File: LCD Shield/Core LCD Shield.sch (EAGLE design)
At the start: 8 parts, among them IC1 MC33269T-5.0, J1 TWIG_2.0-DIP-FEMALE

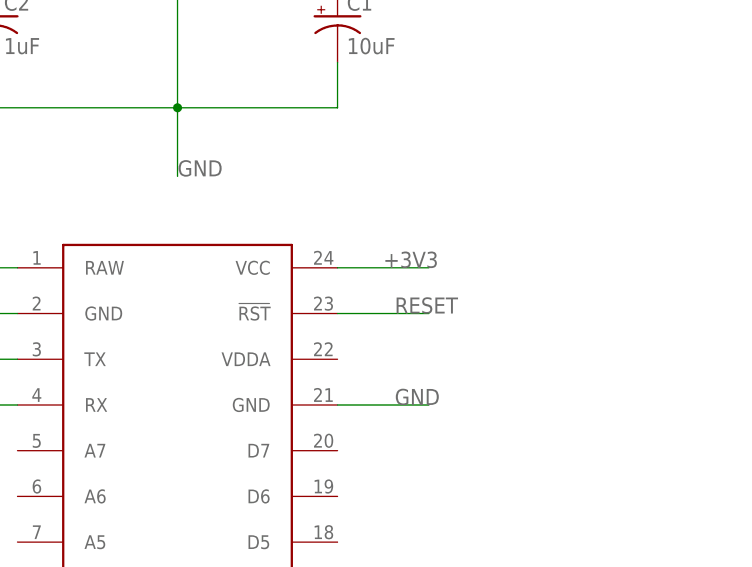
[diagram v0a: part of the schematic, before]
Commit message: Reviewed LCD Shield
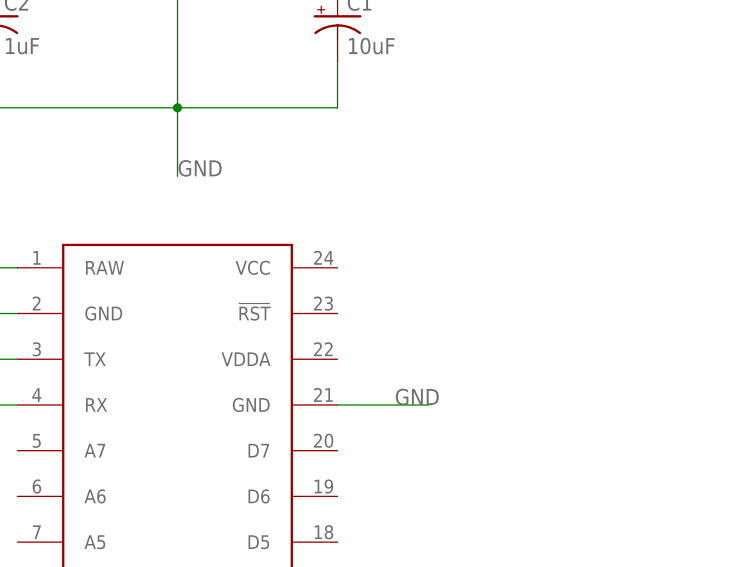
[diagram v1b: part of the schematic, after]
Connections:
- removed net +3V3: U$1.VCC
- removed net RESET: U$1.!RST
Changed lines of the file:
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@@
 <segment>
 <pinref part="IC1" gate="G$1" pin="ADJ"/>
-<wire x1="109.22" y1="124.46" x2="109.22" y2="111.76" width="0.2032" layer="91"/>
+<wire x1="109.22" y1="124.46" x2="109.22" y2="111.76" width="0.1524" layer="91"/>
 <label x="109.22" y="104.14" size="1.778" layer="95"/>
 <pinref part="C2" gate="G$1" pin="-"/>
-<wire x1="109.22" y1="111.76" x2="109.22" y2="104.14" width="0.2032" layer="91"/>
-<wire x1="88.9" y1="116.84" x2="88.9" y2="111.76" width="0.2032" layer="91"/>
-<wire x1="88.9" y1="111.76" x2="109.22" y2="111.76" width="0.2032" layer="91"/>
-<wire x1="109.22" y1="111.76" x2="127" y2="111.76" width="0.2032" layer="91"/>
+<wire x1="109.22" y1="111.76" x2="109.22" y2="104.14" width="0.1524" layer="91"/>
+<wire x1="88.9" y1="116.84" x2="88.9" y2="111.76" width="0.1524" layer="91"/>
+<wire x1="88.9" y1="111.76" x2="109.22" y2="111.76" width="0.1524" layer="91"/>
+<wire x1="109.22" y1="111.76" x2="127" y2="111.76" width="0.1524" layer="91"/>
 <pinref part="C1" gate="G$1" pin="-"/>
-<wire x1="127" y1="111.76" x2="127" y2="116.84" width="0.2032" layer="91"/>
+<wire x1="127" y1="111.76" x2="127" y2="116.84" width="0.1524" layer="91"/>
 <junction x="109.22" y="111.76"/>
 </segment>
 <segment>
 <pinref part="CN1" gate="G$1" pin="1"/>
-<wire x1="43.18" y1="121.92" x2="30.48" y2="121.92" width="0.2032" layer="91"/>
+<wire x1="43.18" y1="121.92" x2="30.48" y2="121.92" width="0.1524" layer="91"/>
 <label x="30.48" y="121.92" size="1.778" layer="95"/>
 </segment>
 <segment>
 <pinref part="JP1" gate="G$1" pin="2"/>
-<wire x1="38.1" y1="134.62" x2="30.48" y2="134.62" width="0.2032" layer="91"/>
+<wire x1="38.1" y1="134.62" x2="30.48" y2="134.62" width="0.1524" layer="91"/>
 <label x="30.48" y="132.08" size="1.778" layer="95"/>
 </segment>
@@
 </segment>
 </net>
-<net name="RESET" class="0">
-<segment>
-<pinref part="U$1" gate="G$1" pin="!RST"/>
-<wire x1="127" y1="88.9" x2="137.16" y2="88.9" width="0.1524" layer="91"/>
-<label x="133.35" y="88.9" size="1.778" layer="95"/>
-</segment>
-</net>
 <net name="VIN" class="0">
 <segment>
@@
 <segment>
 <pinref part="IC1" gate="G$1" pin="VI"/>
-<wire x1="99.06" y1="132.08" x2="88.9" y2="132.08" width="0.2032" layer="91"/>
+<wire x1="99.06" y1="132.08" x2="88.9" y2="132.08" width="0.1524" layer="91"/>
 <label x="68.58" y="132.08" size="1.778" layer="95"/>
 <pinref part="C2" gate="G$1" pin="+"/>
-<wire x1="88.9" y1="132.08" x2="68.58" y2="132.08" width="0.2032" layer="91"/>
-<wire x1="88.9" y1="132.08" x2="88.9" y2="124.46" width="0.2032" layer="91"/>
+<wire x1="88.9" y1="132.08" x2="68.58" y2="132.08" width="0.1524" layer="91"/>
+<wire x1="88.9" y1="132.08" x2="88.9" y2="124.46" width="0.1524" layer="91"/>
 <junction x="88.9" y="132.08"/>
 </segment>
 <segment>
 <pinref part="CN1" gate="G$1" pin="2"/>
-<wire x1="43.18" y1="119.38" x2="30.48" y2="119.38" width="0.2032" layer="91"/>
+<wire x1="43.18" y1="119.38" x2="30.48" y2="119.38" width="0.1524" layer="91"/>
 <label x="30.48" y="116.84" size="1.778" layer="95"/>
 </segment>
 <segment>
 <pinref part="JP1" gate="G$1" pin="1"/>
-<wire x1="38.1" y1="137.16" x2="30.48" y2="137.16" width="0.2032" layer="91"/>
+<wire x1="38.1" y1="137.16" x2="30.48" y2="137.16" width="0.1524" layer="91"/>
 <label x="30.48" y="137.16" size="1.778" layer="95"/>
-</segment>
-</net>
-<net name="+3V3" class="0">
-<segment>
-<pinref part="U$1" gate="G$1" pin="VCC"/>
-<wire x1="127" y1="93.98" x2="137.16" y2="93.98" width="0.1524" layer="91"/>
-<label x="132.08" y="93.98" size="1.778" layer="95"/>
 </segment>
 </net>
@@
 <segment>
 <pinref part="IC1" gate="G$1" pin="VO"/>
-<wire x1="119.38" y1="132.08" x2="127" y2="132.08" width="0.2032" layer="91"/>
+<wire x1="119.38" y1="132.08" x2="127" y2="132.08" width="0.1524" layer="91"/>
 <pinref part="C1" gate="G$1" pin="+"/>
-<wire x1="127" y1="132.08" x2="144.78" y2="132.08" width="0.2032" layer="91"/>
-<wire x1="127" y1="124.46" x2="127" y2="132.08" width="0.2032" layer="91"/>
+<wire x1="127" y1="132.08" x2="144.78" y2="132.08" width="0.1524" layer="91"/>
+<wire x1="127" y1="124.46" x2="127" y2="132.08" width="0.1524" layer="91"/>
 <junction x="127" y="132.08"/>
 <pinref part="S1" gate="1" pin="P"/>

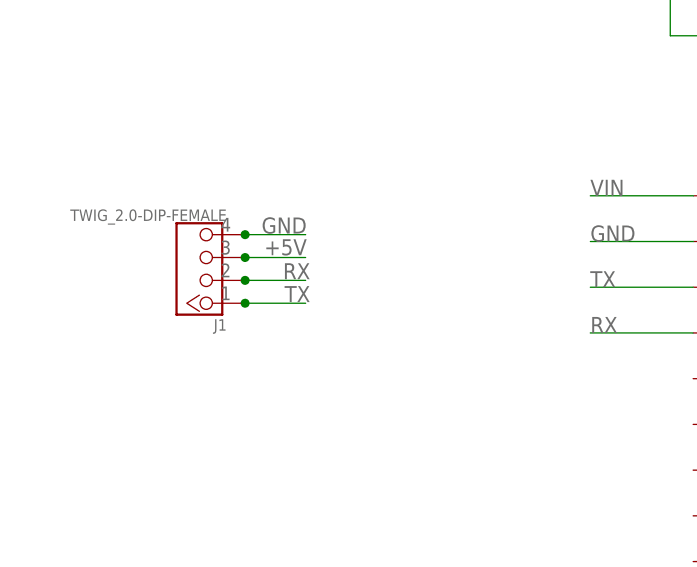
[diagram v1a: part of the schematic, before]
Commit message: Fixed LCD Shield, upgraded to v0.2
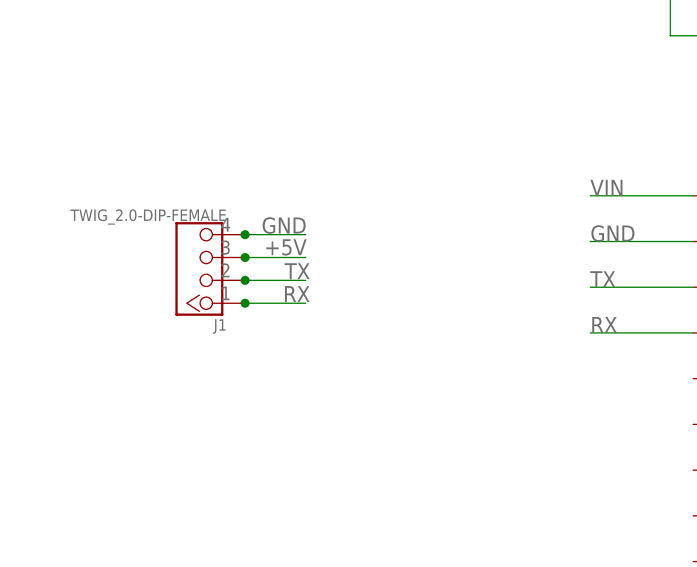
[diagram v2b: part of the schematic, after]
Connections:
- net RX: now also J1.1; no longer J1.2
- net TX: now also J1.2; no longer J1.1
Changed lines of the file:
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@@
 <net name="RX" class="0">
+<segment>
+<pinref part="U$1" gate="G$1" pin="RX"/>
+<wire x1="91.44" y1="78.74" x2="80.01" y2="78.74" width="0.1524" layer="91"/>
+<label x="80.01" y="78.74" size="1.778" layer="95"/>
+</segment>
+<segment>
+<wire x1="48.387" y1="82.042" x2="41.656" y2="82.042" width="0.1524" layer="91"/>
+<wire x1="41.656" y1="82.042" x2="41.529" y2="82.042" width="0.1524" layer="91"/>
+<junction x="41.656" y="82.042"/>
+<label x="48.895" y="82.169" size="1.778" layer="95" rot="MR0"/>
+<pinref part="J1" gate="G$1" pin="1"/>
+</segment>
+</net>
+<net name="TX" class="0">
+<segment>
+<pinref part="U$1" gate="G$1" pin="TX"/>
+<wire x1="91.44" y1="83.82" x2="80.01" y2="83.82" width="0.1524" layer="91"/>
+<label x="80.01" y="83.82" size="1.778" layer="95"/>
+</segment>
 <segment>
 <wire x1="48.387" y1="84.582" x2="41.656" y2="84.582" width="0.1524" layer="91"/>
@@
 <pinref part="J1" gate="G$1" pin="2"/>
 </segment>
-<segment>
-<pinref part="U$1" gate="G$1" pin="RX"/>
-<wire x1="91.44" y1="78.74" x2="80.01" y2="78.74" width="0.1524" layer="91"/>
-<label x="80.01" y="78.74" size="1.778" layer="95"/>
-</segment>
 </net>
-<net name="TX" class="0">
-<segment>
-<wire x1="48.387" y1="82.042" x2="41.656" y2="82.042" width="0.1524" layer="91"/>
-<wire x1="41.656" y1="82.042" x2="41.529" y2="82.042" width="0.1524" layer="91"/>
-<junction x="41.656" y="82.042"/>
-<label x="48.895" y="82.169" size="1.778" layer="95" rot="MR0"/>
-<pinref part="J1" gate="G$1" pin="1"/>
-</segment>
-<segment>
-<pinref part="U$1" gate="G$1" pin="TX"/>
-<wire x1="91.44" y1="83.82" x2="80.01" y2="83.82" width="0.1524" layer="91"/>
-<label x="80.01" y="83.82" size="1.778" layer="95"/>
-</segment>
-</net>
